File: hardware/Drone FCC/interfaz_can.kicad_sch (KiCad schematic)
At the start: 22 parts, among them J17 Conn_01x03, J18 Conn_01x03, J23 Conn_01x03, J26 Conn_01x03, U4 SN65HVD230, U5 SN65HVD230

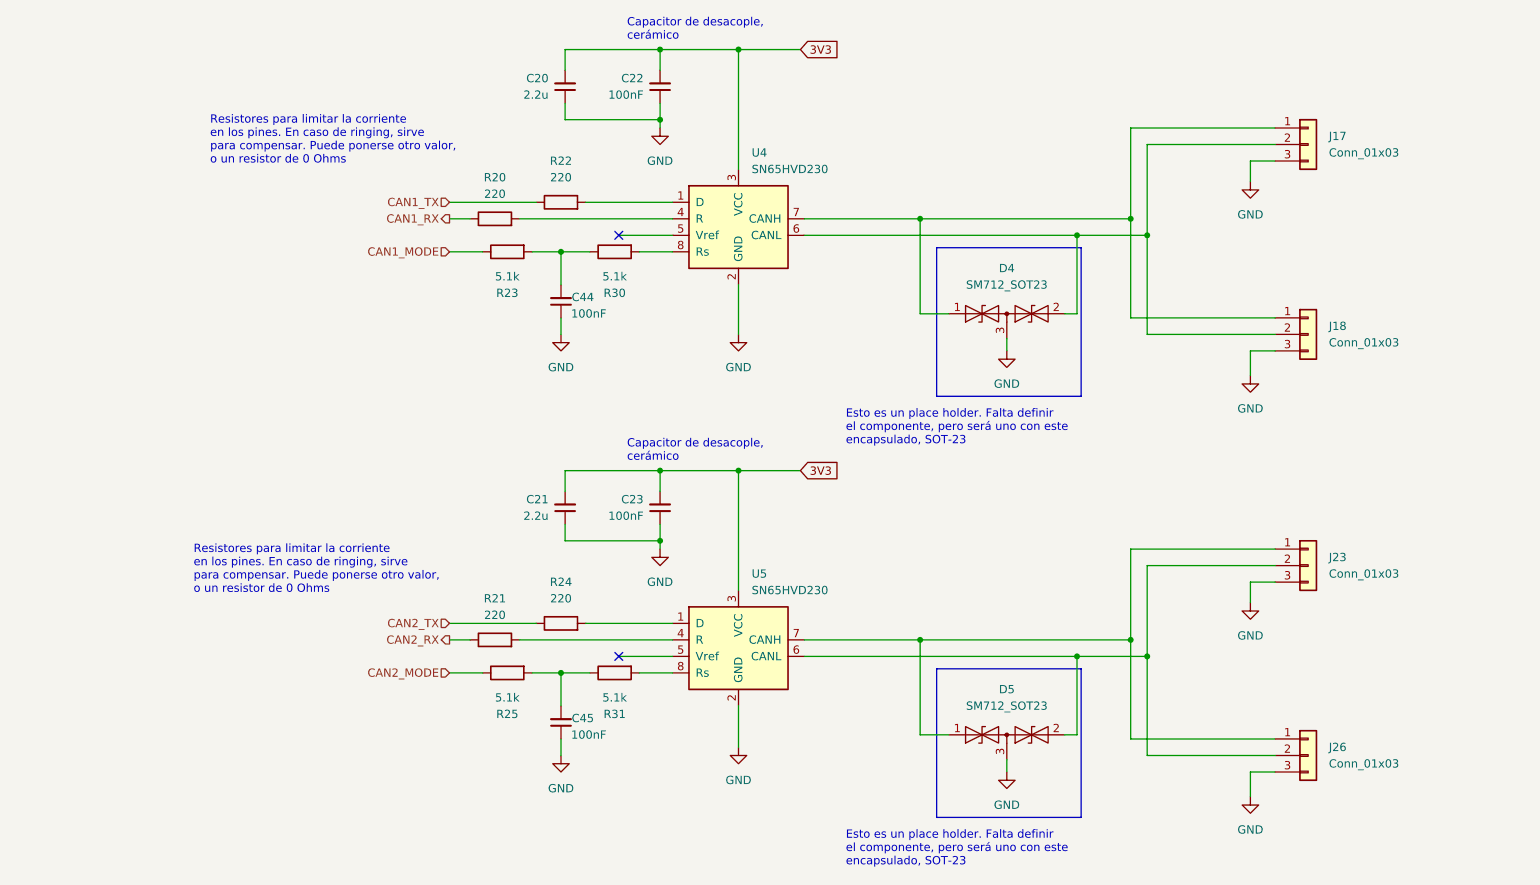
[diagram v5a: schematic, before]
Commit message: re enumeration of components
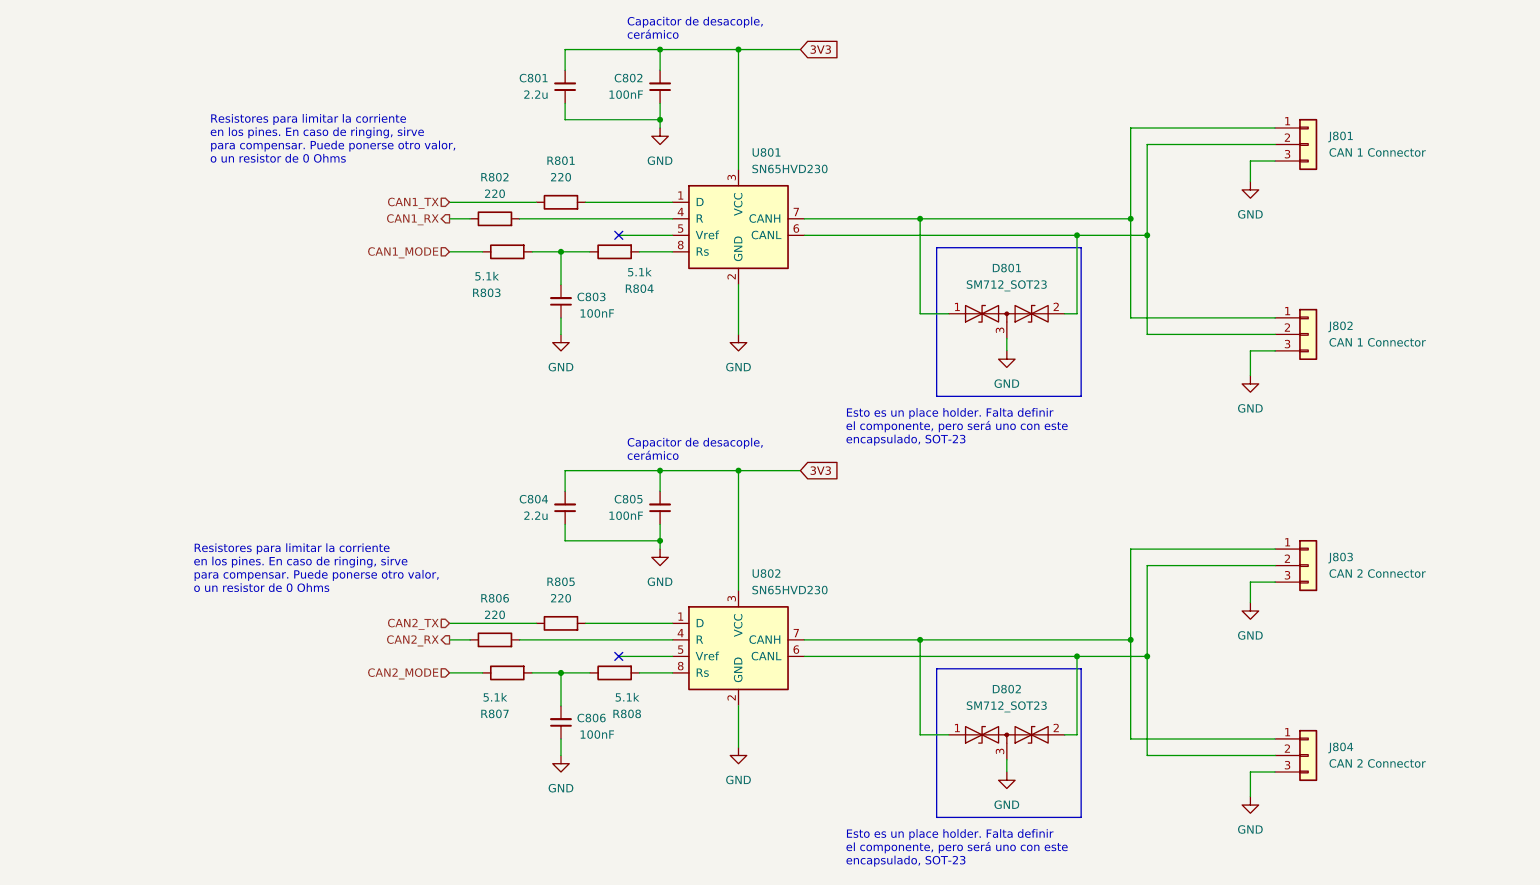
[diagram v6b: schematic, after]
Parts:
- J801: renamed from J17; value Conn_01x03 -> CAN 1 Connector
- J802: renamed from J18; value Conn_01x03 -> CAN 1 Connector
- J803: renamed from J23; value Conn_01x03 -> CAN 2 Connector
- J804: renamed from J26; value Conn_01x03 -> CAN 2 Connector
- renumbered C20 to C801, C22 to C802, C44 to C803, C21 to C804, C23 to C805, C45 to C806, D4 to D801, D5 to D802, R22 to R801, R20 to R802, R23 to R803, R30 to R804, R24 to R805, R21 to R806, R25 to R807, R31 to R808, U4 to U801, U5 to U802
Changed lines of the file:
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@@
   (symbol (lib_id "Device:R") (at 118.11 114.3 90) (unit 1)
     (in_bom yes) (on_board yes) (fields_autoplaced)
-    (property "Reference" "R24" (id 0) (at 118.11 107.95 90))
+    (property "Reference" "R805" (id 0) (at 118.11 107.95 90))
     (property "Value" "220" (id 1) (at 118.11 110.49 90))
     (property "Footprint" "" (id 2) (at 118.11 116.078 90)
@@
   (symbol (lib_id "Interface_CAN_LIN:SN65HVD230") (at 145.415 52.07 0) (unit 1)
     (in_bom yes) (on_board yes) (fields_autoplaced)
-    (property "Reference" "U4" (id 0) (at 147.4344 41.91 0)
+    (property "Reference" "U801" (id 0) (at 147.4344 41.91 0)
       (effects (font (size 1.27 1.27)) (justify left))
     )
@@
   (symbol (lib_id "Diode:SM712_SOT23") (at 186.69 66.675 0) (unit 1)
     (in_bom yes) (on_board yes) (fields_autoplaced)
-    (property "Reference" "D4" (id 0) (at 186.69 59.69 0))
+    (property "Reference" "D801" (id 0) (at 186.69 59.69 0))
     (property "Value" "SM712_SOT23" (id 1) (at 186.69 62.23 0))
     (property "Footprint" "Package_TO_SOT_SMD:SOT-23" (id 2) (at 186.69 75.565 0)
@@
   (symbol (lib_id "Interface_CAN_LIN:SN65HVD230") (at 145.415 116.84 0) (unit 1)
     (in_bom yes) (on_board yes) (fields_autoplaced)
-    (property "Reference" "U5" (id 0) (at 147.4344 106.68 0)
+    (property "Reference" "U802" (id 0) (at 147.4344 106.68 0)
       (effects (font (size 1.27 1.27)) (justify left))
     )
@@
   (symbol (lib_id "Device:R") (at 107.95 52.07 90) (unit 1)
     (in_bom yes) (on_board yes) (fields_autoplaced)
-    (property "Reference" "R20" (id 0) (at 107.95 45.72 90))
+    (property "Reference" "R802" (id 0) (at 107.95 45.72 90))
     (property "Value" "220" (id 1) (at 107.95 48.26 90))
     (property "Footprint" "" (id 2) (at 107.95 53.848 90)
@@
   (symbol (lib_id "Device:C_Small") (at 118.11 64.77 0) (mirror x) (unit 1)
     (in_bom yes) (on_board yes)
-    (property "Reference" "C44" (id 0) (at 123.19 64.135 0)
-      (effects (font (size 1.27 1.27)) (justify right))
-    )
-    (property "Value" "100nF" (id 1) (at 125.095 66.675 0)
+    (property "Reference" "C803" (id 0) (at 125.095 64.135 0)
+      (effects (font (size 1.27 1.27)) (justify right))
+    )
+    (property "Value" "100nF" (id 1) (at 126.365 66.675 0)
       (effects (font (size 1.27 1.27)) (justify right))
     )
@@
   (symbol (lib_id "Device:C_Small") (at 118.745 96.52 0) (mirror x) (unit 1)
     (in_bom yes) (on_board yes) (fields_autoplaced)
-    (property "Reference" "C21" (id 0) (at 116.205 95.2435 0)
+    (property "Reference" "C804" (id 0) (at 116.205 95.2435 0)
       (effects (font (size 1.27 1.27)) (justify right))
     )
@@
   (symbol (lib_id "Device:C_Small") (at 133.35 31.75 0) (mirror x) (unit 1)
     (in_bom yes) (on_board yes) (fields_autoplaced)
-    (property "Reference" "C22" (id 0) (at 130.81 30.4735 0)
+    (property "Reference" "C802" (id 0) (at 130.81 30.4735 0)
       (effects (font (size 1.27 1.27)) (justify right))
     )
@@
   )
   (symbol (lib_id "Device:R") (at 109.855 121.92 90) (mirror x) (unit 1)
-    (in_bom yes) (on_board yes) (fields_autoplaced)
-    (property "Reference" "R25" (id 0) (at 109.855 128.27 90))
-    (property "Value" "5.1k" (id 1) (at 109.855 125.73 90))
+    (in_bom yes) (on_board yes)
+    (property "Reference" "R807" (id 0) (at 107.95 128.27 90))
+    (property "Value" "5.1k" (id 1) (at 107.95 125.73 90))
     (property "Footprint" "" (id 2) (at 109.855 120.142 90)
       (effects (font (size 1.27 1.27)) hide)
@@
   (symbol (lib_id "Device:C_Small") (at 118.745 31.75 0) (mirror x) (unit 1)
     (in_bom yes) (on_board yes) (fields_autoplaced)
-    (property "Reference" "C20" (id 0) (at 116.205 30.4735 0)
+    (property "Reference" "C801" (id 0) (at 116.205 30.4735 0)
       (effects (font (size 1.27 1.27)) (justify right))
     )
@@
   (symbol (lib_id "Device:C_Small") (at 118.11 129.54 0) (mirror x) (unit 1)
     (in_bom yes) (on_board yes)
-    (property "Reference" "C45" (id 0) (at 123.19 128.905 0)
-      (effects (font (size 1.27 1.27)) (justify right))
-    )
-    (property "Value" "100nF" (id 1) (at 125.095 131.445 0)
+    (property "Reference" "C806" (id 0) (at 125.095 128.905 0)
+      (effects (font (size 1.27 1.27)) (justify right))
+    )
+    (property "Value" "100nF" (id 1) (at 126.365 131.445 0)
       (effects (font (size 1.27 1.27)) (justify right))
     )
@@
   )
   (symbol (lib_id "Device:R") (at 109.855 57.15 90) (mirror x) (unit 1)
-    (in_bom yes) (on_board yes) (fields_autoplaced)
-    (property "Reference" "R23" (id 0) (at 109.855 63.5 90))
-    (property "Value" "5.1k" (id 1) (at 109.855 60.96 90))
+    (in_bom yes) (on_board yes)
+    (property "Reference" "R803" (id 0) (at 106.68 63.5 90))
+    (property "Value" "5.1k" (id 1) (at 106.68 60.96 90))
     (property "Footprint" "" (id 2) (at 109.855 55.372 90)
       (effects (font (size 1.27 1.27)) hide)
@@
   (symbol (lib_id "Device:R") (at 107.95 116.84 90) (unit 1)
     (in_bom yes) (on_board yes) (fields_autoplaced)
-    (property "Reference" "R21" (id 0) (at 107.95 110.49 90))
+    (property "Reference" "R806" (id 0) (at 107.95 110.49 90))
     (property "Value" "220" (id 1) (at 107.95 113.03 90))
     (property "Footprint" "" (id 2) (at 107.95 118.618 90)
@@
   (symbol (lib_id "Device:C_Small") (at 133.35 96.52 0) (mirror x) (unit 1)
     (in_bom yes) (on_board yes) (fields_autoplaced)
-    (property "Reference" "C23" (id 0) (at 130.81 95.2435 0)
+    (property "Reference" "C805" (id 0) (at 130.81 95.2435 0)
       (effects (font (size 1.27 1.27)) (justify right))
     )
@@
   (symbol (lib_id "Diode:SM712_SOT23") (at 186.69 131.445 0) (unit 1)
     (in_bom yes) (on_board yes) (fields_autoplaced)
-    (property "Reference" "D5" (id 0) (at 186.69 124.46 0))
+    (property "Reference" "D802" (id 0) (at 186.69 124.46 0))
     (property "Value" "SM712_SOT23" (id 1) (at 186.69 127 0))
     (property "Footprint" "Package_TO_SOT_SMD:SOT-23" (id 2) (at 186.69 140.335 0)
@@
   (symbol (lib_id "Connector_Generic:Conn_01x03") (at 233.045 69.85 0) (unit 1)
     (in_bom yes) (on_board yes) (fields_autoplaced)
-    (property "Reference" "J18" (id 0) (at 236.22 68.5799 0)
-      (effects (font (size 1.27 1.27)) (justify left))
-    )
-    (property "Value" "Conn_01x03" (id 1) (at 236.22 71.1199 0)
+    (property "Reference" "J802" (id 0) (at 236.22 68.5799 0)
+      (effects (font (size 1.27 1.27)) (justify left))
+    )
+    (property "Value" "CAN 1 Connector" (id 1) (at 236.22 71.1199 0)
       (effects (font (size 1.27 1.27)) (justify left))
     )
@@
   )
   (symbol (lib_id "Device:R") (at 126.365 57.15 90) (mirror x) (unit 1)
-    (in_bom yes) (on_board yes) (fields_autoplaced)
-    (property "Reference" "R30" (id 0) (at 126.365 63.5 90))
-    (property "Value" "5.1k" (id 1) (at 126.365 60.96 90))
+    (in_bom yes) (on_board yes)
+    (property "Reference" "R804" (id 0) (at 130.175 62.865 90))
+    (property "Value" "5.1k" (id 1) (at 130.175 60.325 90))
     (property "Footprint" "" (id 2) (at 126.365 55.372 90)
       (effects (font (size 1.27 1.27)) hide)
@@
   (symbol (lib_id "Connector_Generic:Conn_01x03") (at 233.045 40.64 0) (unit 1)
     (in_bom yes) (on_board yes) (fields_autoplaced)
-    (property "Reference" "J17" (id 0) (at 236.22 39.3699 0)
-      (effects (font (size 1.27 1.27)) (justify left))
-    )
-    (property "Value" "Conn_01x03" (id 1) (at 236.22 41.9099 0)
+    (property "Reference" "J801" (id 0) (at 236.22 39.3699 0)
+      (effects (font (size 1.27 1.27)) (justify left))
+    )
+    (property "Value" "CAN 1 Connector" (id 1) (at 236.22 41.9099 0)
       (effects (font (size 1.27 1.27)) (justify left))
     )
@@
   (symbol (lib_id "Connector_Generic:Conn_01x03") (at 233.045 105.41 0) (unit 1)
     (in_bom yes) (on_board yes) (fields_autoplaced)
-    (property "Reference" "J23" (id 0) (at 236.22 104.1399 0)
-      (effects (font (size 1.27 1.27)) (justify left))
-    )
-    (property "Value" "Conn_01x03" (id 1) (at 236.22 106.6799 0)
+    (property "Reference" "J803" (id 0) (at 236.22 104.1399 0)
+      (effects (font (size 1.27 1.27)) (justify left))
+    )
+    (property "Value" "CAN 2 Connector" (id 1) (at 236.22 106.6799 0)
       (effects (font (size 1.27 1.27)) (justify left))
     )
@@
   )
   (symbol (lib_id "Device:R") (at 126.365 121.92 90) (mirror x) (unit 1)
-    (in_bom yes) (on_board yes) (fields_autoplaced)
-    (property "Reference" "R31" (id 0) (at 126.365 128.27 90))
-    (property "Value" "5.1k" (id 1) (at 126.365 125.73 90))
+    (in_bom yes) (on_board yes)
+    (property "Reference" "R808" (id 0) (at 128.27 128.27 90))
+    (property "Value" "5.1k" (id 1) (at 128.27 125.73 90))
     (property "Footprint" "" (id 2) (at 126.365 120.142 90)
       (effects (font (size 1.27 1.27)) hide)
@@
   (symbol (lib_id "Device:R") (at 118.11 49.53 90) (unit 1)
     (in_bom yes) (on_board yes) (fields_autoplaced)
-    (property "Reference" "R22" (id 0) (at 118.11 43.18 90))
+    (property "Reference" "R801" (id 0) (at 118.11 43.18 90))
     (property "Value" "220" (id 1) (at 118.11 45.72 90))
     (property "Footprint" "" (id 2) (at 118.11 51.308 90)
@@
   (symbol (lib_id "Connector_Generic:Conn_01x03") (at 233.045 134.62 0) (unit 1)
     (in_bom yes) (on_board yes) (fields_autoplaced)
-    (property "Reference" "J26" (id 0) (at 236.22 133.3499 0)
-      (effects (font (size 1.27 1.27)) (justify left))
-    )
-    (property "Value" "Conn_01x03" (id 1) (at 236.22 135.8899 0)
-      (effects (font (size 1.27 1.27)) (justify left))
-    )
+    (property "Reference" "J804" (id 0) (at 236.22 133.3499 0)
+      (effects (font (size 1.27 1.27)) (justify left))
+    )
+    (property "Value" "CAN 2 Connector" (id 1) (at 236.22 135.8899 0)
+      (effects (font (size 1.27 1.27)) (justify left))
+    )

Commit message: start routing
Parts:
- removed J801, J802: CAN 1 Connector, DF13A-3P-1.25H(21):HRS_DF13A-3P-1.25H(21), symbol Connector_Generic:Conn_01x03
- removed J803, J804: CAN 2 Connector, DF13A-3P-1.25H(21):HRS_DF13A-3P-1.25H(21), symbol Connector_Generic:Conn_01x03
- added J801: CAN 1 Connector 1, DF13A-3P-1.25H(21):HRS_DF13A-3P-1.25H(21), symbol DF13A-3P-1.25H(21):HRS_DF13A-3P-1.25H(21)
- added J802: CAN 1 Connector 2, DF13A-3P-1.25H(21):HRS_DF13A-3P-1.25H(21), symbol DF13A-3P-1.25H(21):HRS_DF13A-3P-1.25H(21)
- added J803: CAN 2 Connector 1, DF13A-3P-1.25H(21):HRS_DF13A-3P-1.25H(21), symbol DF13A-3P-1.25H(21):HRS_DF13A-3P-1.25H(21)
- added J804: CAN 2 Connector 2, DF13A-3P-1.25H(21):HRS_DF13A-3P-1.25H(21), symbol DF13A-3P-1.25H(21):HRS_DF13A-3P-1.25H(21)
- C801, C802, C804, C805: footprint (none) -> Capacitor_SMD:C_0603_1608Metric_Pad1.08x0.95mm_HandSolder
- C803, C806: footprint (none) -> Capacitor_SMD:C_0402_1005Metric_Pad0.74x0.62mm_HandSolder
- R801, R802, R803, R804, R805, R806, R807, R808: footprint (none) -> Resistor_SMD:R_0402_1005Metric_Pad0.72x0.64mm_HandSolder
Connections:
- net GND: now also J801.3, J801.S1 (SHIELD), J801.S2 (SHIELD), J802.3, J802.S1 (SHIELD), J802.S2 (SHIELD), J803.3, J803.S1 (SHIELD), J803.S2 (SHIELD), J804.3, J804.S1 (SHIELD), J804.S2 (SHIELD)
- net at D801.2 (A2), U801.6 (CANL): now also J801.2, J802.2
- net at D801.1 (A1), U801.7 (CANH): now also J801.1, J802.1
- net at D802.2 (A2), U802.6 (CANL): now also J803.2, J804.2
- net at D802.1 (A1), U802.7 (CANH): now also J803.1, J804.1
